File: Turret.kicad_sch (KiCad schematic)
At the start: 25 parts, among them J1 Conn_01x04_Pin, J10 Conn_01x02_Pin, J12 Conn_01x02_Pin, J13 Conn_01x04_Pin, J14 Conn_01x04_Pin, J15 Conn_01x08_Pin, J2 Conn_01x02_Pin, J20 Conn_01x02_Pin, J21 Conn_01x02_Pin, J3 Conn_01x02_Pin, J4 Conn_01x02_Pin, J5 Conn_01x04_Pin, J6 Conn_01x02_Pin, J7 Conn_01x02_Pin, J8 Conn_01x02_Pin, J9 Conn_01x02_Pin

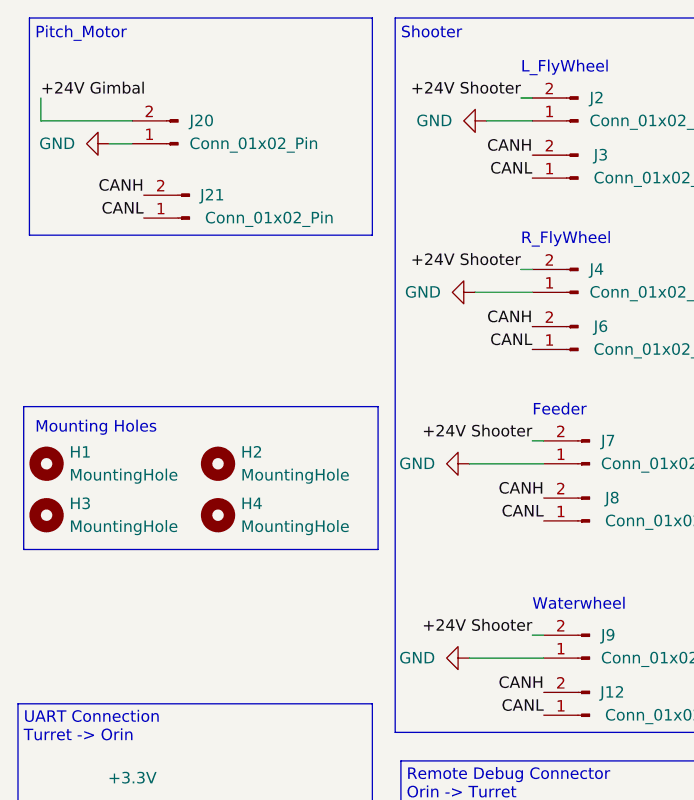
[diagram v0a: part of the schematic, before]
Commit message: Fixed net names in schematic, initial pcb layout
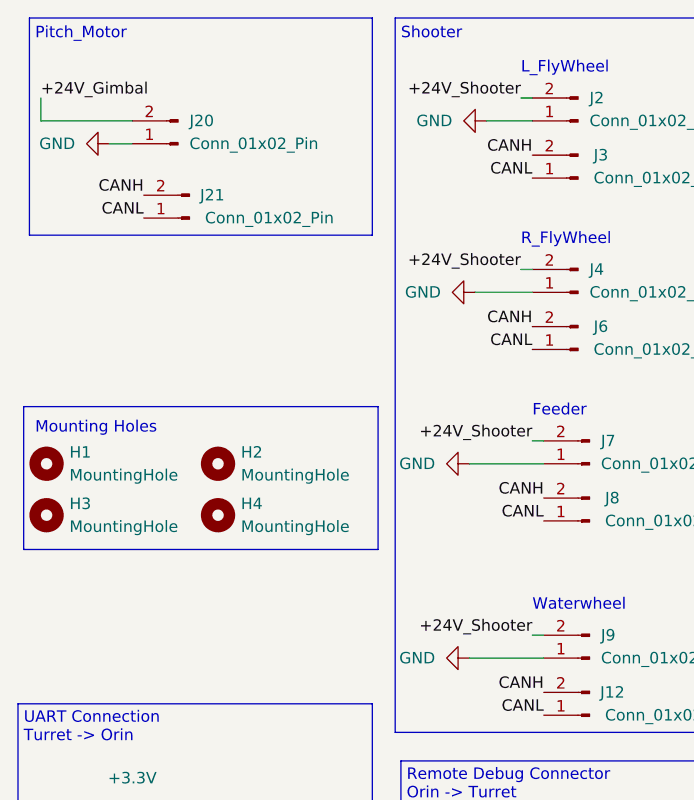
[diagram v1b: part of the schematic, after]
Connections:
- net +24V Gimbal is gone; now on net +24V_Gimbal: J20.2 (Pin_2)
- net +24V Shooter is gone; now on net +24V_Shooter: J2.2 (Pin_2), J4.2 (Pin_2), J7.2 (Pin_2), J9.2 (Pin_2)
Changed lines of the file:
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@@
     (effects (font (size 1.27 1.27)) (justify right bottom))
   )
-  (label "+24V Shooter" (at 78.74 95.885 180) (fields_autoplaced)
+  (label "+24V_Shooter" (at 78.74 95.885 180) (fields_autoplaced)
     (effects (font (size 1.27 1.27)) (justify right bottom))
   )
@@
     (effects (font (size 1.27 1.27)) (justify right bottom))
   )
-  (label "+24V Shooter" (at 77.47 36.195 180) (fields_autoplaced)
+  (label "+24V_Shooter" (at 77.47 36.195 180) (fields_autoplaced)
     (effects (font (size 1.27 1.27)) (justify right bottom))
   )
@@
     (effects (font (size 1.27 1.27)) (justify right bottom))
   )
-  (label "+24V Shooter" (at 77.47 55.245 180) (fields_autoplaced)
+  (label "+24V_Shooter" (at 77.47 55.245 180) (fields_autoplaced)
     (effects (font (size 1.27 1.27)) (justify right bottom))
   )
@@
     (effects (font (size 1.27 1.27)) (justify right bottom))
   )
-  (label "+24V Gimbal" (at 24.13 36.195 0) (fields_autoplaced)
+  (label "+24V_Gimbal" (at 24.13 36.195 0) (fields_autoplaced)
     (effects (font (size 1.27 1.27)) (justify left bottom))
   )
@@
     (effects (font (size 1.27 1.27)) (justify right bottom))
   )
-  (label "+24V Shooter" (at 78.74 74.295 180) (fields_autoplaced)
+  (label "+24V_Shooter" (at 78.74 74.295 180) (fields_autoplaced)
     (effects (font (size 1.27 1.27)) (justify right bottom))
   )

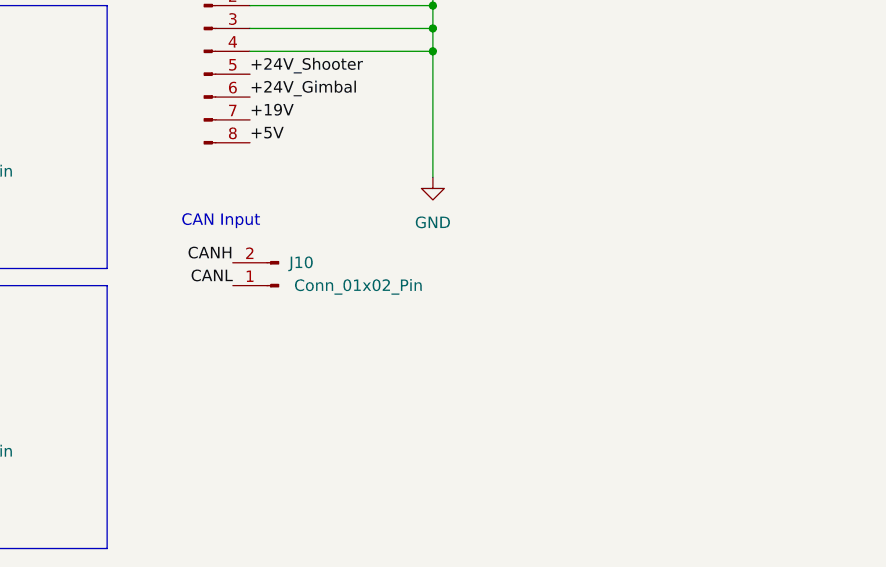
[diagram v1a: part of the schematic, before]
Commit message: Adding new ref system, other push now deprecated
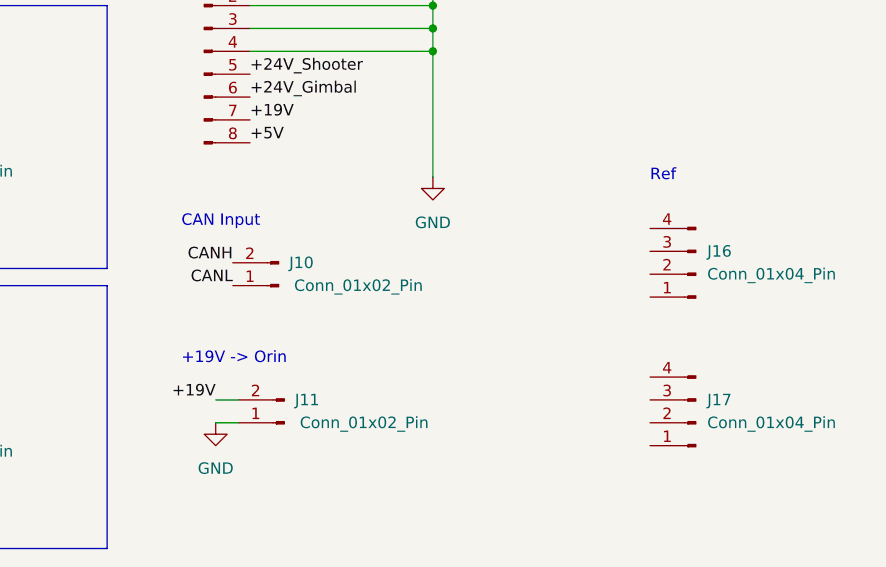
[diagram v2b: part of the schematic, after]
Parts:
- added J11: Conn_01x02_Pin, Connector_AMASS:AMASS_XT30U-F_1x02_P5.0mm_Vertical, symbol Connector:Conn_01x02_Pin
- added J16, J17: Conn_01x04_Pin, Connector_JST:JST_GH_BM04B-GHS-TBT_1x04-1MP_P1.25mm_Vertical, symbol Connector:Conn_01x04_Pin
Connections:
- net +19V: now also J11.2 (Pin_2)
- net GND: now also J11.1 (Pin_1)
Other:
- note added: "+19V -> Orin"
- note added: "Ref"

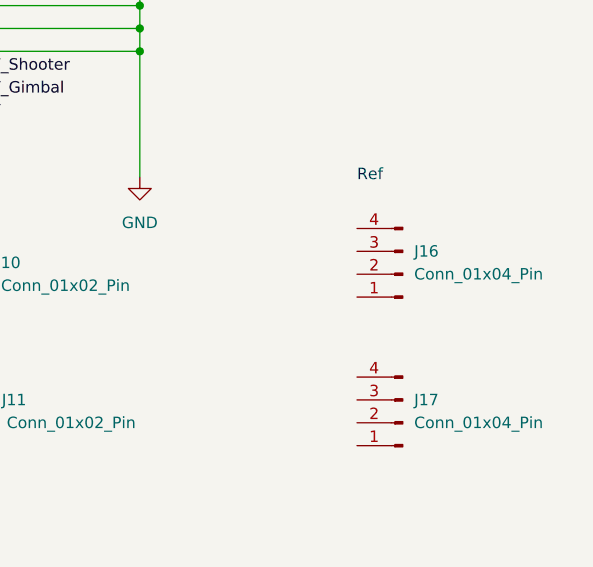
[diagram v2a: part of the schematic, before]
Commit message: New layout, test points not final
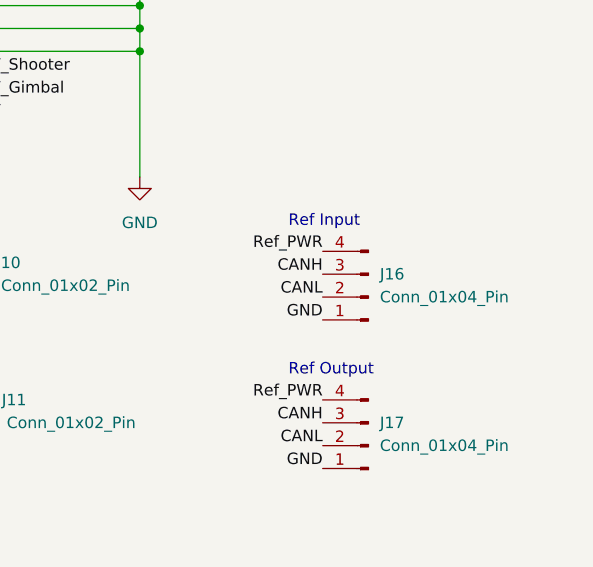
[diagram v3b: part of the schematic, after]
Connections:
- net CANH: now also J16.3 (Pin_3), J17.3 (Pin_3)
- net CANL: now also J16.2 (Pin_2), J17.2 (Pin_2)
- net GND: now also J16.1 (Pin_1), J17.1 (Pin_1)
- net Ref_PWR: now reaches J16.4 (Pin_4)
- net Ref_PWR: now also J17.4 (Pin_4)
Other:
- note added: "Ref Input"
- note added: "Ref Output"
- note removed: "Ref"
- moved on the sheet: J16, J17
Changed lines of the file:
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@@
     (fill (type none))
   )
-  (text "Ref" (at 163.83 129.54 0)
+  (text "Ref Input\n" (at 156.21 134.62 0)
     (effects (font (size 1.27 1.27)) (justify left bottom))
   )
@@
     (effects (font (size 1.27 1.27)) (justify left bottom))
   )
+  (text "Ref Output\n" (at 156.21 151.13 0)
+    (effects (font (size 1.27 1.27)) (justify left bottom))
+  )
   (text "Shooter" (at 64.135 29.845 0)
     (effects (font (size 1.27 1.27)) (justify left bottom))
@@
     (effects (font (size 1.27 1.27)) (justify right bottom))
   )
+  (label "CANL" (at 160.02 142.24 180) (fields_autoplaced)
+    (effects (font (size 1.27 1.27)) (justify right bottom))
+  )
   (label "SWDIO" (at 70.485 159.385 180) (fields_autoplaced)
     (effects (font (size 1.27 1.27)) (justify right bottom))
@@
     (effects (font (size 1.27 1.27)) (justify right bottom))
   )
+  (label "CANH" (at 160.02 139.7 180) (fields_autoplaced)
+    (effects (font (size 1.27 1.27)) (justify right bottom))
+  )
   (label "CANH" (at 35.56 46.99 180) (fields_autoplaced)
     (effects (font (size 1.27 1.27)) (justify right bottom))
@@
     (effects (font (size 1.27 1.27)) (justify right bottom))
   )
+  (label "CANH" (at 160.02 156.21 180) (fields_autoplaced)
+    (effects (font (size 1.27 1.27)) (justify right bottom))
+  )
   (label "CANL" (at 35.56 49.53 180) (fields_autoplaced)
     (effects (font (size 1.27 1.27)) (justify right bottom))
@@
     (effects (font (size 1.27 1.27)) (justify right bottom))
   )
+  (label "Ref_PWR" (at 160.02 153.67 180) (fields_autoplaced)
+    (effects (font (size 1.27 1.27)) (justify right bottom))
+  )
   (label "UART_TX" (at 36.195 124.46 180) (fields_autoplaced)
     (effects (font (size 1.27 1.27)) (justify right bottom))
   )
+  (label "CANL" (at 160.02 158.75 180) (fields_autoplaced)
+    (effects (font (size 1.27 1.27)) (justify right bottom))
+  )
   (label "UART_TX" (at 36.195 158.75 180) (fields_autoplaced)
     (effects (font (size 1.27 1.27)) (justify right bottom))
@@
     (effects (font (size 1.27 1.27)) (justify right bottom))
   )
+  (label "GND" (at 160.02 144.78 180) (fields_autoplaced)
+    (effects (font (size 1.27 1.27)) (justify right bottom))
+  )
   (label "+19V" (at 119.38 122.555 0) (fields_autoplaced)
     (effects (font (size 1.27 1.27)) (justify left bottom))
@@
     (effects (font (size 1.27 1.27)) (justify left bottom))
   )
+  (label "GND" (at 160.02 161.29 180) (fields_autoplaced)
+    (effects (font (size 1.27 1.27)) (justify right bottom))
+  )
   (label "SWCLK" (at 70.485 156.845 180) (fields_autoplaced)
     (effects (font (size 1.27 1.27)) (justify right bottom))
@@
   )
   (label "+24V_Shooter" (at 78.74 74.295 180) (fields_autoplaced)
+    (effects (font (size 1.27 1.27)) (justify right bottom))
+  )
+  (label "Ref_PWR" (at 160.02 137.16 180) (fields_autoplaced)
     (effects (font (size 1.27 1.27)) (justify right bottom))
   )
@@
     )
   )
-  (symbol (lib_id "Connector:Conn_01x04_Pin") (at 168.91 139.7 180) (unit 1)
-    (in_bom yes) (on_board yes) (dnp no) (fields_autoplaced)
-    (property "Reference" "J16" (at 170.18 137.16 0)
-      (effects (font (size 1.27 1.27)) (justify right))
-    )
-    (property "Value" "Conn_01x04_Pin" (at 170.18 139.7 0)
-      (effects (font (size 1.27 1.27)) (justify right))
-    )
-    (property "Footprint" "Connector_JST:JST_GH_BM04B-GHS-TBT_1x04-1MP_P1.25mm_Vertical" (at 168.91 139.7 0)
-      (effects (font (size 1.27 1.27)) hide)
-    )
-    (property "Datasheet" "~" (at 168.91 139.7 0)
+  (symbol (lib_id "Connector:Conn_01x04_Pin") (at 165.1 142.24 180) (unit 1)
+    (in_bom yes) (on_board yes) (dnp no) (fields_autoplaced)
+    (property "Reference" "J16" (at 166.37 139.7 0)
+      (effects (font (size 1.27 1.27)) (justify right))
+    )
+    (property "Value" "Conn_01x04_Pin" (at 166.37 142.24 0)
+      (effects (font (size 1.27 1.27)) (justify right))
+    )
+    (property "Footprint" "Connector_JST:JST_GH_BM04B-GHS-TBT_1x04-1MP_P1.25mm_Vertical" (at 165.1 142.24 0)
+      (effects (font (size 1.27 1.27)) hide)
+    )
+    (property "Datasheet" "~" (at 165.1 142.24 0)
       (effects (font (size 1.27 1.27)) hide)
     )
@@
     )
   )
-  (symbol (lib_id "Connector:Conn_01x04_Pin") (at 168.91 156.21 180) (unit 1)
-    (in_bom yes) (on_board yes) (dnp no) (fields_autoplaced)
-    (property "Reference" "J17" (at 170.18 153.67 0)
-      (effects (font (size 1.27 1.27)) (justify right))
-    )
-    (property "Value" "Conn_01x04_Pin" (at 170.18 156.21 0)
-      (effects (font (size 1.27 1.27)) (justify right))
-    )
-    (property "Footprint" "Connector_JST:JST_GH_BM04B-GHS-TBT_1x04-1MP_P1.25mm_Vertical" (at 168.91 156.21 0)
-      (effects (font (size 1.27 1.27)) hide)
-    )
-    (property "Datasheet" "~" (at 168.91 156.21 0)
-      (effects (font (size 1.27 1.27)) hide)
-    )
+  (symbol (lib_id "Connector:Conn_01x04_Pin") (at 165.1 158.75 180) (unit 1)
+    (in_bom yes) (on_board yes) (dnp no) (fields_autoplaced)
+    (property "Reference" "J17" (at 166.37 156.21 0)
+      (effects (font (size 1.27 1.27)) (justify right))
+    )
+    (property "Value" "Conn_01x04_Pin" (at 166.37 158.75 0)
+      (effects (font (size 1.27 1.27)) (justify right))
+    )
+    (property "Footprint" "Connector_JST:JST_GH_BM04B-GHS-TBT_1x04-1MP_P1.25mm_Vertical" (at 165.1 158.75 0)
+      (effects (font (size 1.27 1.27)) hide)
+    )
+    (property "Datasheet" "~" (at 165.1 158.75 0)
+      (effects (font (size 1.27 1.27)) hide)
+    )

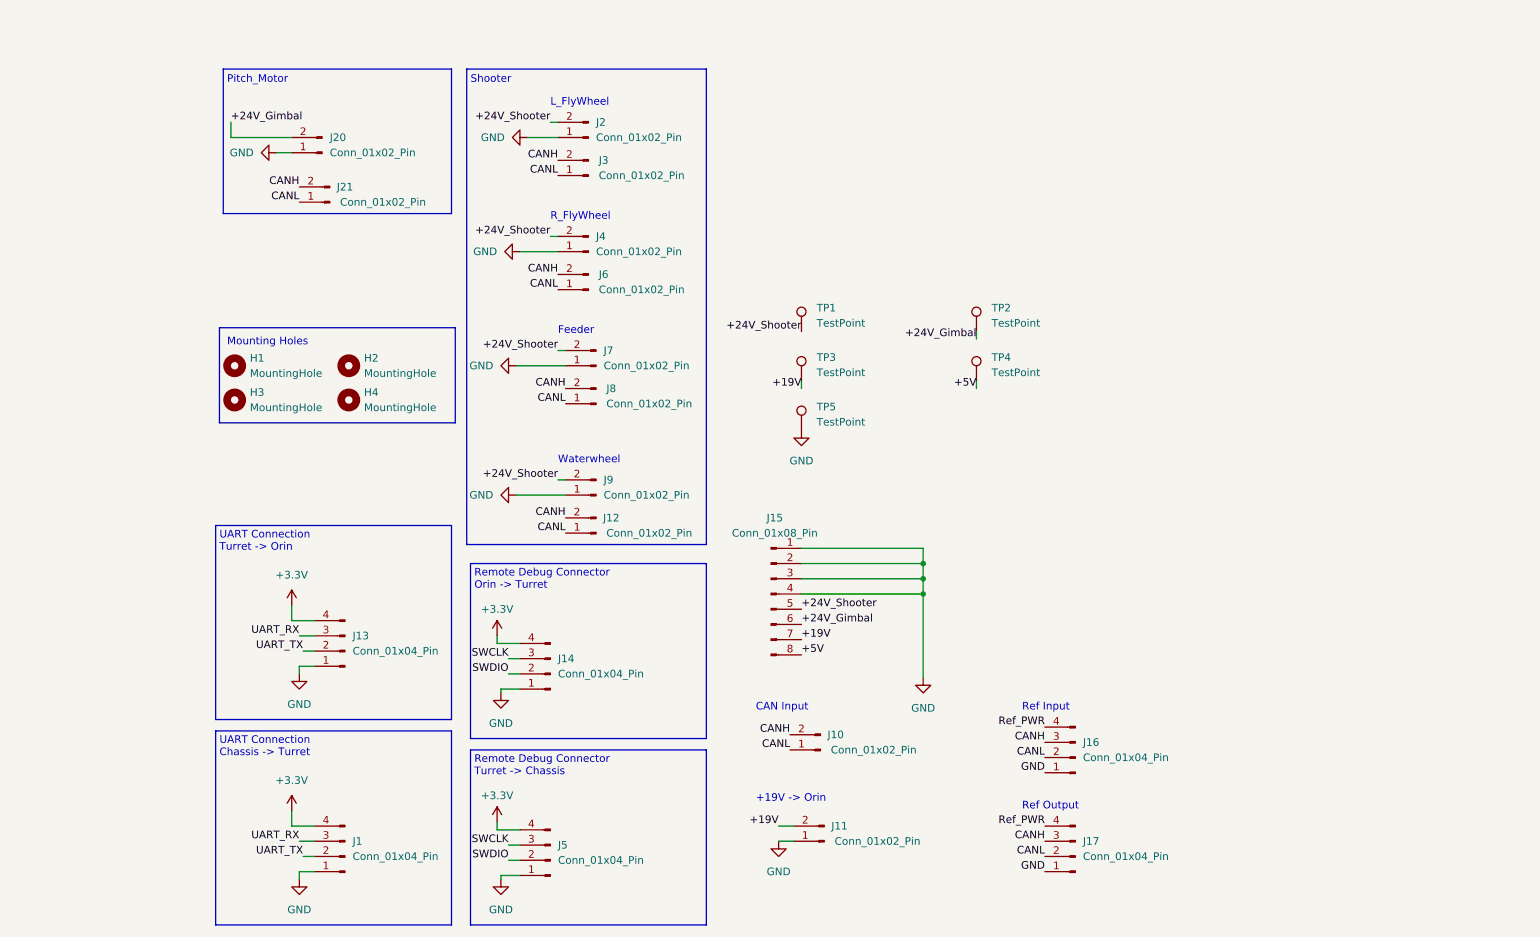
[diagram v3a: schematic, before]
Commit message: Tried to fix footprints, also changed to traces for testpoints
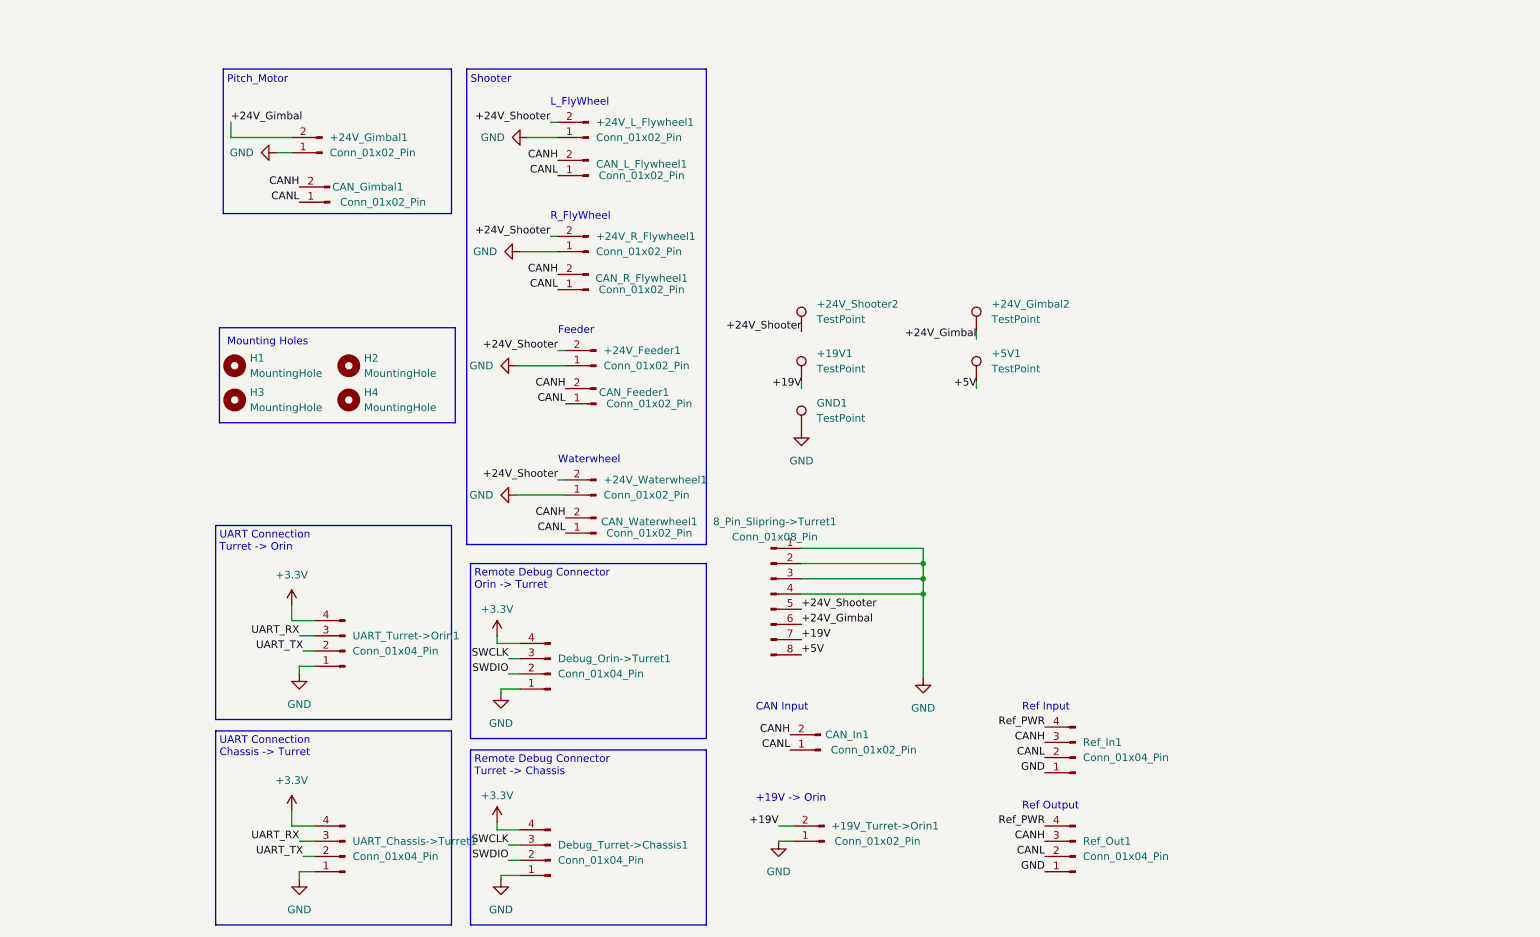
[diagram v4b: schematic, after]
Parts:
- +19V_Turret->Orin1: renamed from J11; footprint Connector_AMASS:AMASS_XT30U-F_1x02_P5.0mm_Vertical -> Robomaster_ICs:AMASS_XT30U-F_1x02_P5.0mm_Vertical_copy
- +24V_Feeder1: renamed from J7; footprint Connector_AMASS:AMASS_XT30U-F_1x02_P5.0mm_Vertical -> Robomaster_ICs:AMASS_XT30U-F_1x02_P5.0mm_Vertical_copy
- +24V_Gimbal1: renamed from J20; footprint Connector_AMASS:AMASS_XT30U-F_1x02_P5.0mm_Vertical -> Robomaster_ICs:AMASS_XT30U-F_1x02_P5.0mm_Vertical_copy
- +24V_L_Flywheel1: renamed from J2; footprint Connector_AMASS:AMASS_XT30U-F_1x02_P5.0mm_Vertical -> Robomaster_ICs:AMASS_XT30U-F_1x02_P5.0mm_Vertical_copy
- +24V_R_Flywheel1: renamed from J4; footprint Connector_AMASS:AMASS_XT30U-F_1x02_P5.0mm_Vertical -> Robomaster_ICs:AMASS_XT30U-F_1x02_P5.0mm_Vertical_copy
- +24V_Waterwheel1: renamed from J9; footprint Connector_AMASS:AMASS_XT30U-F_1x02_P5.0mm_Vertical -> Robomaster_ICs:AMASS_XT30U-F_1x02_P5.0mm_Vertical_copy
- renumbered TP3 to +19V1, TP2 to +24V_Gimbal2, TP1 to +24V_Shooter2, TP4 to +5V1, J15 to 8_Pin_Slipring->Turret1, J8 to CAN_Feeder1, J21 to CAN_Gimbal1, J10 to CAN_In1, J3 to CAN_L_Flywheel1, J6 to CAN_R_Flywheel1, J12 to CAN_Waterwheel1, J14 to Debug_Orin->Turret1, J5 to Debug_Turret->Chassis1, TP5 to GND1, J16 to Ref_In1, J17 to Ref_Out1, J1 to UART_Chassis->Turret1, J13 to UART_Turret->Orin1
